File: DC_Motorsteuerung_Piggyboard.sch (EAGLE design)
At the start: 12 parts, among them X1 PFVERB10

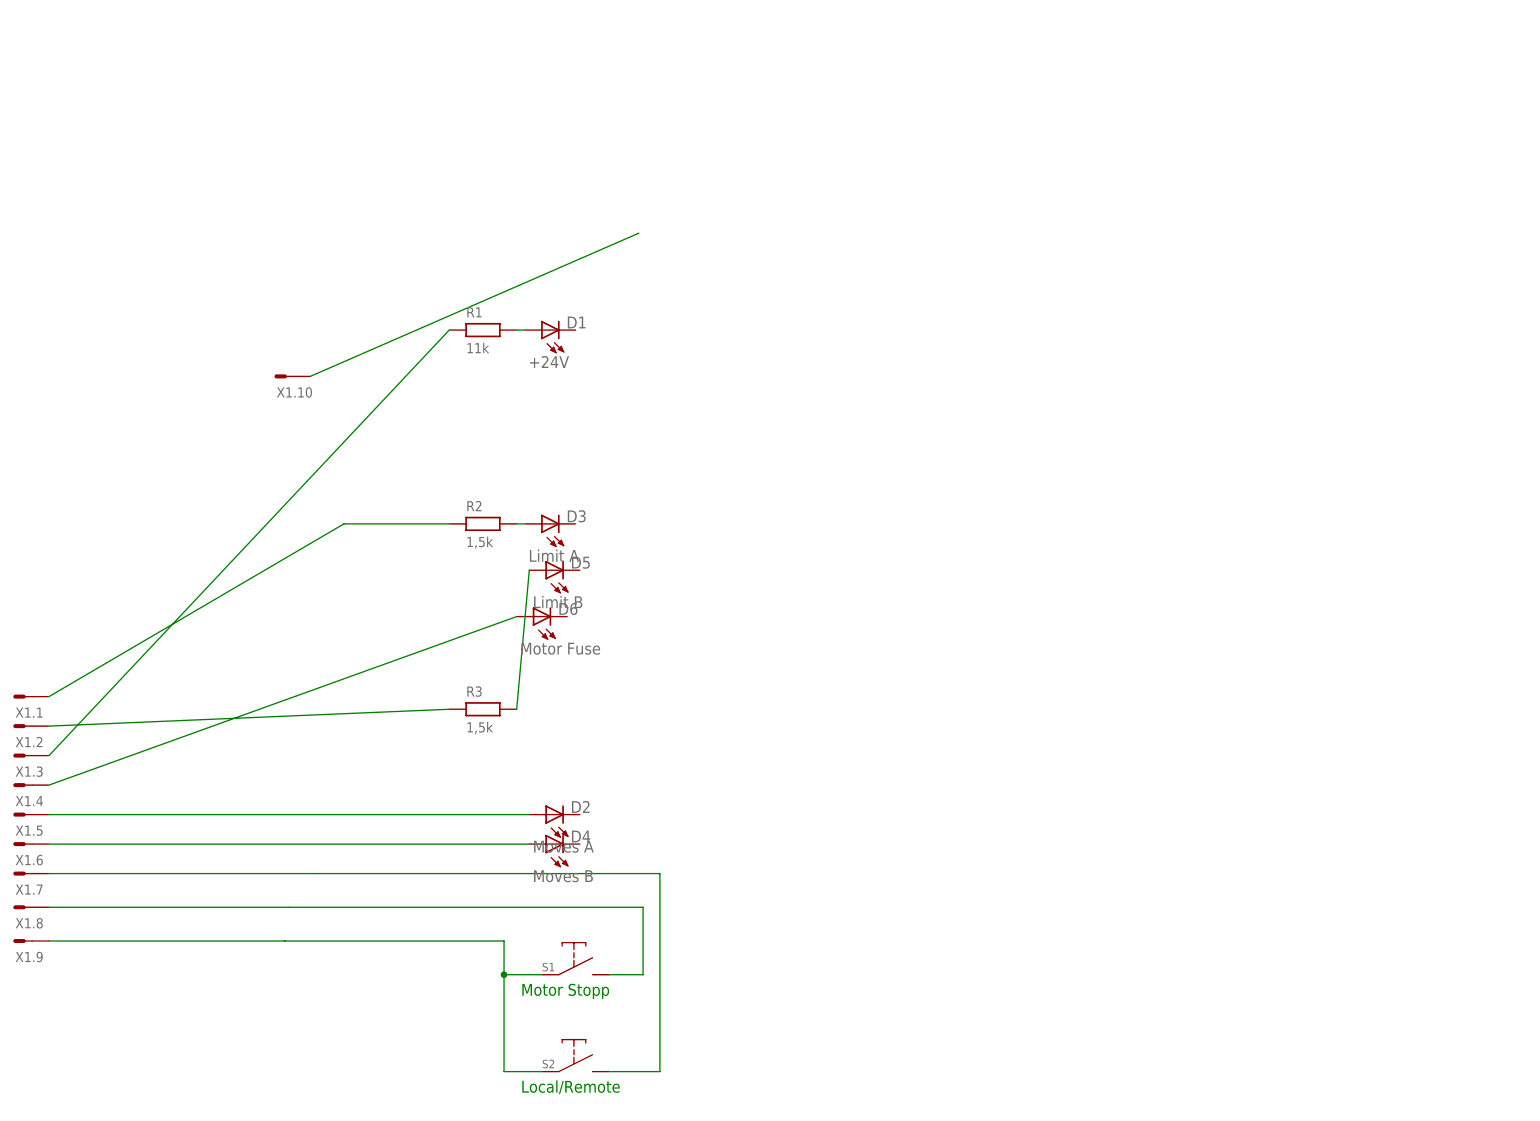
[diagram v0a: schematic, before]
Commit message: Schaltplan fast fertiggestellt.
Umschalter (Taster s2) fehlt
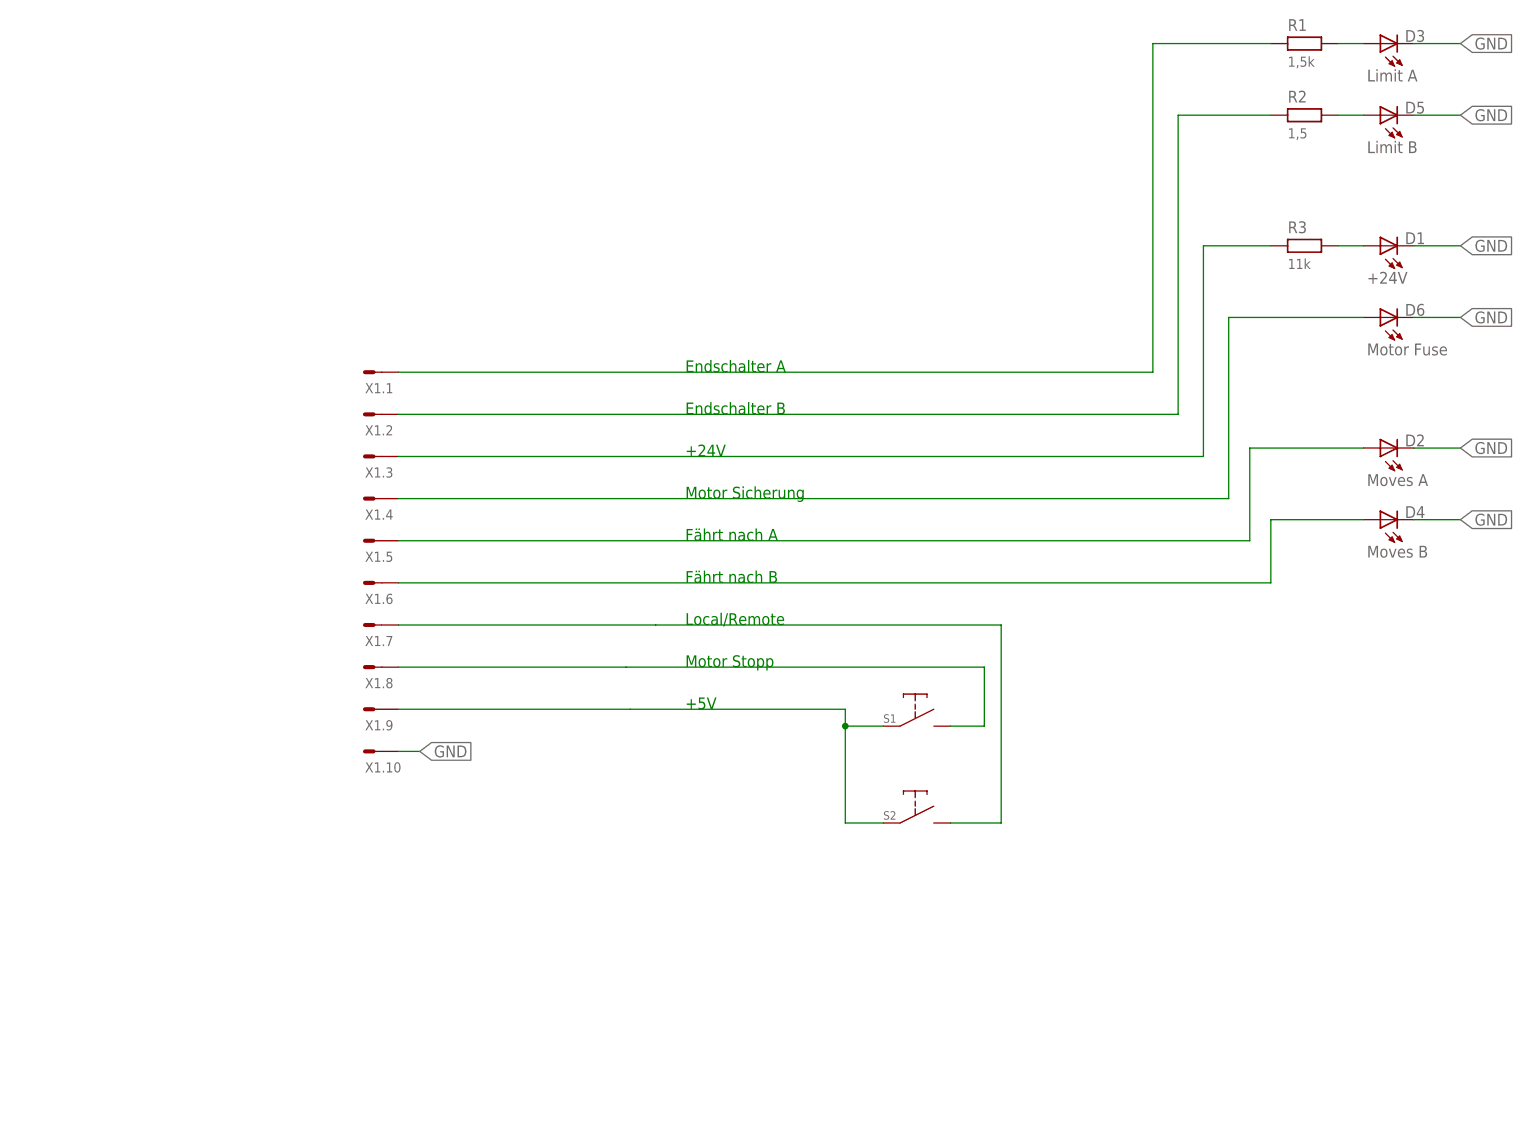
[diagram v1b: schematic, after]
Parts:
- R1: value 11k -> 1,5k; device Resistor:0805 -> Resistor:R_0,4W
- R2: value 1,5k -> 1,5; device Resistor:0805 -> Resistor:R_0,4W
- R3: value 1,5k -> 11k; device Resistor:0805 -> Resistor:R_0,4W
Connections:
- net FAEHRTNACHA renamed N$12
- net FAEHRTNACHB renamed N$11
- net MOTORSICHERUNGLED renamed N$5
- removed net N$10: X1.10.1
- removed net N$5 (its old number): D1.A, R1.2
- new net GND: D1.C, D2.C, D3.C, D4.C, D5.C, D6.C, X1.10.1
- new net N$13: D1.A, R3.2
- net N$1: now also X1.2.1; no longer X1.1.1
- net N$2: now also R1.2; no longer R2.2
- net N$3: now also R1.1, X1.1.1; no longer R3.1, X1.2.1
- net N$4: now also R2.2; no longer R3.2
- net N$6: now also R3.1; no longer R1.1
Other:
- note added: "+24V"
- note added: "+5V"
- note added: "Endschalter A"
- note added: "Endschalter B"
- note added: "Fährt nach A"
- note added: "Fährt nach B"
- note added: "Motor Sicherung"
- moved on the sheet: D1, D2, D3, D4, D5, D6, R1, R2, R3, S1, S2, X1.1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

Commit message: Piggyboard updated
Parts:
- added H1: Das Loch 3,2 kilometer, Holes:MOUNT-HOLE3.2
- added R4, R5, R6: 1,5, Resistor:R_0,4W
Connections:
- new net N$10: D4.A, R6.2
- new net N$14: D2.A, R5.2
- new net N$15: D6.A, R4.2
- net N$11: now also R6.1; no longer D4.A
- net N$12: now also R5.1; no longer D2.A
- net N$5: now also R4.1; no longer D6.A
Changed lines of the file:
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@@
 <setting verticaltext="up"/>
 </settings>
-<grid distance="0.635" unitdist="mm" unit="mm" style="dots" multiple="1" display="yes" altdistance="0.3175" altunitdist="mm" altunit="mm"/>
+<grid distance="0.635" unitdist="mm" unit="mm" style="dots" multiple="1" display="yes" altdistance="0.01" altunitdist="inch" altunit="mm"/>
 <layers>
-<layer number="1" name="Top" color="4" fill="1" visible="yes" active="no"/>
-<layer number="2" name="Route2" color="1" fill="3" visible="yes" active="no"/>
-<layer number="3" name="Route3" color="4" fill="3" visible="yes" active="no"/>
-<layer number="4" name="Route4" color="1" fill="4" visible="yes" active="no"/>
-<layer number="5" name="Route5" color="4" fill="4" visible="yes" active="no"/>
-<layer number="6" name="Route6" color="1" fill="8" visible="yes" active="no"/>
-<layer number="7" name="Route7" color="4" fill="8" visible="yes" active="no"/>
-<layer number="8" name="Route8" color="1" fill="2" visible="yes" active="no"/>
-<layer number="9" name="Route9" color="4" fill="2" visible="yes" active="no"/>
-<layer number="10" name="Route10" color="1" fill="7" visible="yes" active="no"/>
-<layer number="11" name="Route11" color="4" fill="7" visible="yes" active="no"/>
-<layer number="12" name="Route12" color="1" fill="5" visible="yes" active="no"/>
-<layer number="13" name="Route13" color="4" fill="5" visible="yes" active="no"/>
-<layer number="14" name="Route14" color="1" fill="6" visible="yes" active="no"/>
-<layer number="15" name="Route15" color="4" fill="6" visible="yes" active="no"/>
-<layer number="16" name="Bottom" color="1" fill="1" visible="yes" active="no"/>
-<layer number="17" name="Pads" color="2" fill="1" visible="yes" active="no"/>
-<layer number="18" name="Vias" color="3" fill="1" visible="yes" active="no"/>
-<layer number="19" name="Unrouted" color="14" fill="1" visible="yes" active="no"/>
-<layer number="20" name="Dimension" color="15" fill="1" visible="yes" active="no"/>
-<layer number="21" name="tPlace" color="7" fill="1" visible="yes" active="no"/>
-<layer number="22" name="bPlace" color="7" fill="1" visible="yes" active="no"/>
-<layer number="23" name="tOrigins" color="15" fill="1" visible="yes" active="no"/>
-<layer number="24" name="bOrigins" color="15" fill="1" visible="yes" active="no"/>
-<layer number="25" name="tNames" color="7" fill="1" visible="yes" active="no"/>
-<layer number="26" name="bNames" color="7" fill="1" visible="yes" active="no"/>
-<layer number="27" name="tValues" color="7" fill="1" visible="yes" active="no"/>
-<layer number="28" name="bValues" color="7" fill="1" visible="yes" active="no"/>
+<layer number="1" name="Top" color="4" fill="1" visible="no" active="no"/>
+<layer number="2" name="Route2" color="1" fill="3" visible="no" active="no"/>
+<layer number="3" name="Route3" color="4" fill="3" visible="no" active="no"/>
+<layer number="4" name="Route4" color="1" fill="4" visible="no" active="no"/>
+<layer number="5" name="Route5" color="4" fill="4" visible="no" active="no"/>
+<layer number="6" name="Route6" color="1" fill="8" visible="no" active="no"/>
+<layer number="7" name="Route7" color="4" fill="8" visible="no" active="no"/>
+<layer number="8" name="Route8" color="1" fill="2" visible="no" active="no"/>
+<layer number="9" name="Route9" color="4" fill="2" visible="no" active="no"/>
+<layer number="10" name="Route10" color="1" fill="7" visible="no" active="no"/>
+<layer number="11" name="Route11" color="4" fill="7" visible="no" active="no"/>
+<layer number="12" name="Route12" color="1" fill="5" visible="no" active="no"/>
+<layer number="13" name="Route13" color="4" fill="5" visible="no" active="no"/>
+<layer number="14" name="Route14" color="1" fill="6" visible="no" active="no"/>
+<layer number="15" name="Route15" color="4" fill="6" visible="no" active="no"/>
+<layer number="16" name="Bottom" color="1" fill="1" visible="no" active="no"/>
+<layer number="17" name="Pads" color="2" fill="1" visible="no" active="no"/>
+<layer number="18" name="Vias" color="3" fill="1" visible="no" active="no"/>
+<layer number="19" name="Unrouted" color="14" fill="1" visible="no" active="no"/>
+<layer number="20" name="Dimension" color="15" fill="1" visible="no" active="no"/>
+<layer number="21" name="tPlace" color="7" fill="1" visible="no" active="no"/>
+<layer number="22" name="bPlace" color="7" fill="1" visible="no" active="no"/>
+<layer number="23" name="tOrigins" color="15" fill="1" visible="no" active="no"/>
+<layer number="24" name="bOrigins" color="15" fill="1" visible="no" active="no"/>
+<layer number="25" name="tNames" color="7" fill="1" visible="no" active="no"/>
+<layer number="26" name="bNames" color="7" fill="1" visible="no" active="no"/>
+<layer number="27" name="tValues" color="7" fill="1" visible="no" active="no"/>
+<layer number="28" name="bValues" color="7" fill="1" visible="no" active="no"/>
 <layer number="29" name="tStop" color="7" fill="3" visible="no" active="no"/>
 <layer number="30" name="bStop" color="7" fill="6" visible="no" active="no"/>
@@
 <layer number="35" name="tGlue" color="7" fill="4" visible="no" active="no"/>
 <layer number="36" name="bGlue" color="7" fill="5" visible="no" active="no"/>
-<layer number="37" name="tTest" color="7" fill="1" visible="yes" active="no"/>
-<layer number="38" name="bTest" color="7" fill="1" visible="yes" active="no"/>
+<layer number="37" name="tTest" color="7" fill="1" visible="no" active="no"/>
+<layer number="38" name="bTest" color="7" fill="1" visible="no" active="no"/>
 <layer number="39" name="tKeepout" color="4" fill="11" visible="no" active="no"/>
 <layer number="40" name="bKeepout" color="1" fill="11" visible="no" active="no"/>
@@
 <layer number="44" name="Drills" color="7" fill="1" visible="no" active="no"/>
 <layer number="45" name="Holes" color="7" fill="1" visible="no" active="no"/>
-<layer number="46" name="Milling" color="3" fill="1" visible="yes" active="no"/>
-<layer number="47" name="Measures" color="7" fill="1" visible="yes" active="no"/>
-<layer number="48" name="Document" color="7" fill="1" visible="yes" active="no"/>
-<layer number="49" name="Reference" color="7" fill="1" visible="yes" active="no"/>
-<layer number="50" name="dxf" color="7" fill="1" visible="yes" active="no"/>
-<layer number="51" name="tDocu" color="7" fill="1" visible="yes" active="no"/>
-<layer number="52" name="bDocu" color="7" fill="1" visible="yes" active="no"/>
+<layer number="46" name="Milling" color="3" fill="1" visible="no" active="no"/>
+<layer number="47" name="Measures" color="7" fill="1" visible="no" active="no"/>
+<layer number="48" name="Document" color="7" fill="1" visible="no" active="no"/>
+<layer number="49" name="Reference" color="7" fill="1" visible="no" active="no"/>
+<layer number="50" name="dxf" color="7" fill="1" visible="no" active="no"/>
+<layer number="51" name="tDocu" color="7" fill="1" visible="no" active="no"/>
+<layer number="52" name="bDocu" color="7" fill="1" visible="no" active="no"/>
 <layer number="91" name="Nets" color="2" fill="1" visible="yes" active="yes"/>
 <layer number="92" name="Busses" color="1" fill="1" visible="yes" active="yes"/>
@@
 <part name="R2" library="Resistor" deviceset="R_0,4W" device="" value="1,5"/>
 <part name="R3" library="Resistor" deviceset="R_0,4W" device="" value="11k"/>
+<part name="R4" library="Resistor" deviceset="R_0,4W" device="" value="1,5"/>
+<part name="R5" library="Resistor" deviceset="R_0,4W" device="" value="1,5"/>
+<part name="R6" library="Resistor" deviceset="R_0,4W" device="" value="1,5"/>
+<part name="H1" library="Holes" deviceset="MOUNT-HOLE" device="3.2" value="Das Loch 3,2 kilometer"/>
 </parts>
 <sheets>
@@
 <instance part="R2" gate="G$1" x="250.19" y="207.645"/>
 <instance part="R3" gate="G$1" x="250.19" y="187.96"/>
+<instance part="R4" gate="G$1" x="250.19" y="177.165"/>
+<instance part="R5" gate="G$1" x="250.19" y="157.48"/>
+<instance part="R6" gate="G$1" x="250.19" y="146.685"/>
+<instance part="H1" gate="G$1" x="238.125" y="114.3"/>
 </instances>
 <busses>
@@
 <wire x1="113.665" y1="137.16" x2="245.11" y2="137.16" width="0.1524" layer="91"/>
 <wire x1="245.11" y1="137.16" x2="245.11" y2="146.685" width="0.1524" layer="91"/>
-<pinref part="D4" gate="G$1" pin="A"/>
-<wire x1="245.11" y1="146.685" x2="259.08" y2="146.685" width="0.1524" layer="91"/>
+<pinref part="R6" gate="G$1" pin="1"/>
 </segment>
 </net>
@@
 <wire x1="113.665" y1="143.51" x2="241.935" y2="143.51" width="0.1524" layer="91"/>
 <wire x1="241.935" y1="143.51" x2="241.935" y2="157.48" width="0.1524" layer="91"/>
-<pinref part="D2" gate="G$1" pin="A"/>
-<wire x1="241.935" y1="157.48" x2="259.08" y2="157.48" width="0.1524" layer="91"/>
+<pinref part="R5" gate="G$1" pin="1"/>
+<wire x1="245.11" y1="157.48" x2="241.935" y2="157.48" width="0.1524" layer="91"/>
 </segment>
 </net>
@@
 <wire x1="113.665" y1="149.86" x2="238.76" y2="149.86" width="0.1524" layer="91"/>
 <wire x1="238.76" y1="149.86" x2="238.76" y2="177.165" width="0.1524" layer="91"/>
-<pinref part="D6" gate="G$1" pin="A"/>
-<wire x1="238.76" y1="177.165" x2="259.08" y2="177.165" width="0.1524" layer="91"/>
+<pinref part="R4" gate="G$1" pin="1"/>
+<wire x1="245.11" y1="177.165" x2="238.76" y2="177.165" width="0.1524" layer="91"/>
 </segment>
 </net>
@@
 </segment>
 </net>
+<net name="N$10" class="0">
+<segment>
+<pinref part="R6" gate="G$1" pin="2"/>
+<pinref part="D4" gate="G$1" pin="A"/>
+<wire x1="255.27" y1="146.685" x2="259.08" y2="146.685" width="0.1524" layer="91"/>
+</segment>
+</net>
+<net name="N$14" class="0">
+<segment>
+<pinref part="D2" gate="G$1" pin="A"/>
+<pinref part="R5" gate="G$1" pin="2"/>
+<wire x1="259.08" y1="157.48" x2="255.27" y2="157.48" width="0.1524" layer="91"/>
+</segment>
+</net>
+<net name="N$15" class="0">
+<segment>
+<pinref part="R4" gate="G$1" pin="2"/>
+<pinref part="D6" gate="G$1" pin="A"/>
+<wire x1="255.27" y1="177.165" x2="259.08" y2="177.165" width="0.1524" layer="91"/>
+</segment>
+</net>

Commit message: Piggyboard updated
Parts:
- removed S2: (no value), Switch:DRUCKTASTER_ABGW
- added U$2: UMSCHALTER_SINGLE_POLE, Test:UMSCHALTER_SINGLE_POLE
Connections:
- net GND: now also U$2.2
- net N$8: now also U$2.3; no longer S2.C
- net N$9: now also U$2.1; no longer S2.N0
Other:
- moved on the sheet: H1
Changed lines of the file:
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@@
 <setting verticaltext="up"/>
 </settings>
-<grid distance="0.635" unitdist="mm" unit="mm" style="dots" multiple="1" display="yes" altdistance="0.01" altunitdist="inch" altunit="mm"/>
+<grid distance="0.635" unitdist="mm" unit="mm" style="dots" multiple="1" display="yes" altdistance="0.3175" altunitdist="mm" altunit="mm"/>
 <layers>
 <layer number="1" name="Top" color="4" fill="1" visible="no" active="no"/>
@@
 <part name="X1" library="Connector" deviceset="PFVERB10" device=""/>
 <part name="S1" library="Switch" deviceset="DRUCKTASTER" device="_ABGW" value="MotorStopp"/>
-<part name="S2" library="Switch" deviceset="DRUCKTASTER" device="_ABGW"/>
 <part name="R1" library="Resistor" deviceset="R_0,4W" device="" value="1,5k"/>
 <part name="R2" library="Resistor" deviceset="R_0,4W" device="" value="1,5"/>
@@
 <part name="R6" library="Resistor" deviceset="R_0,4W" device="" value="1,5"/>
 <part name="H1" library="Holes" deviceset="MOUNT-HOLE" device="3.2" value="Das Loch 3,2 kilometer"/>
+<part name="U$2" library="Test" deviceset="UMSCHALTER_SINGLE_POLE" device=""/>
 </parts>
 <sheets>
@@
 <attribute name="NAME" x="186.69" y="116.078" size="1.27" layer="95" font="vector"/>
 </instance>
-<instance part="S2" gate="G$1" x="191.77" y="103.505" smashed="yes">
-<attribute name="NAME" x="186.69" y="101.473" size="1.27" layer="95" font="vector"/>
-</instance>
 <instance part="R1" gate="G$1" x="250.19" y="218.44"/>
 <instance part="R2" gate="G$1" x="250.19" y="207.645"/>
@@
 <instance part="R5" gate="G$1" x="250.19" y="157.48"/>
 <instance part="R6" gate="G$1" x="250.19" y="146.685"/>
-<instance part="H1" gate="G$1" x="238.125" y="114.3"/>
+<instance part="H1" gate="G$1" x="188.595" y="61.595"/>
+<instance part="U$2" gate="G$1" x="222.25" y="120.65"/>
 </instances>
 <busses>
@@
 <wire x1="148.59" y1="118.11" x2="113.665" y2="118.11" width="0.1524" layer="91"/>
 <wire x1="148.59" y1="118.11" x2="180.975" y2="118.11" width="0.1524" layer="91"/>
-<pinref part="S2" gate="G$1" pin="C"/>
-<wire x1="186.69" y1="100.965" x2="180.975" y2="100.965" width="0.1524" layer="91"/>
-<wire x1="180.975" y1="100.965" x2="180.975" y2="115.57" width="0.1524" layer="91"/>
+<wire x1="180.975" y1="109.855" x2="180.975" y2="115.57" width="0.1524" layer="91"/>
 <pinref part="S1" gate="G$1" pin="C"/>
 <wire x1="180.975" y1="115.57" x2="180.975" y2="118.11" width="0.1524" layer="91"/>
 <wire x1="186.69" y1="115.57" x2="180.975" y2="115.57" width="0.1524" layer="91"/>
 <junction x="180.975" y="115.57"/>
+<wire x1="180.975" y1="109.855" x2="180.975" y2="107.315" width="0.1524" layer="91"/>
+<wire x1="180.975" y1="107.315" x2="229.87" y2="107.315" width="0.1524" layer="91"/>
+<wire x1="229.87" y1="107.315" x2="229.87" y2="115.57" width="0.1524" layer="91"/>
+<pinref part="U$2" gate="G$1" pin="3"/>
 </segment>
 </net>
@@
 <pinref part="X1" gate=".7" pin="1"/>
 <wire x1="113.665" y1="130.81" x2="152.4" y2="130.81" width="0.1524" layer="91"/>
-<wire x1="152.4" y1="130.81" x2="204.47" y2="130.81" width="0.1524" layer="91"/>
-<wire x1="204.47" y1="130.81" x2="204.47" y2="100.965" width="0.1524" layer="91"/>
-<pinref part="S2" gate="G$1" pin="N0"/>
-<wire x1="204.47" y1="100.965" x2="196.85" y2="100.965" width="0.1524" layer="91"/>
+<wire x1="152.4" y1="130.81" x2="207.01" y2="130.81" width="0.1524" layer="91"/>
+<wire x1="207.01" y1="130.81" x2="207.01" y2="120.65" width="0.1524" layer="91"/>
+<wire x1="207.01" y1="120.65" x2="212.09" y2="120.65" width="0.1524" layer="91"/>
+<pinref part="U$2" gate="G$1" pin="1"/>
 </segment>
 </net>
@@
 <label x="273.685" y="146.685" size="1.778" layer="95" font="vector" xref="yes"/>
 </segment>
-</net>
+<segment>
+<wire x1="229.87" y1="125.73" x2="231.775" y2="125.73" width="0.1524" layer="91"/>
+<wire x1="231.775" y1="125.73" x2="232.41" y2="125.73" width="0.1524" layer="91"/>
+<label x="232.41" y="125.73" size="1.778" layer="95" font="vector" xref="yes"/>
+<pinref part="U$2" gate="G$1" pin="2"/>
+</segment>
+</net>
